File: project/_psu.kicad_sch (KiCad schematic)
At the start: 45 parts, among them J301 5V, J302 24V, J303 3V3, U301 ME3121AM6G, U302 MT3406

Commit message: fixing silk and bom and generating prod/doc files
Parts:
- F301: jlc-part-type (none) -> E; lcsc# (none) -> C22378353
- J301, J302, J303: jlc-part-type (none) -> -; now in the parts list
- L301, L302: jlc-part-type (none) -> E; lcsc# (none) -> C241467
- R301, R302, R312: jlc-part-type B -> E; lcsc# (none) -> C127687
- R303: lcsc# (none) -> C17470
- R304, R313, R314, R316: lcsc# (none) -> C17713
- R305, R306, R307, R315: lcsc# (none) -> C17414
- R308, R309, R310, R311: lcsc# (none) -> C17673
- U302: jlc-part-type (none) -> E; lcsc# (none) -> C22462728

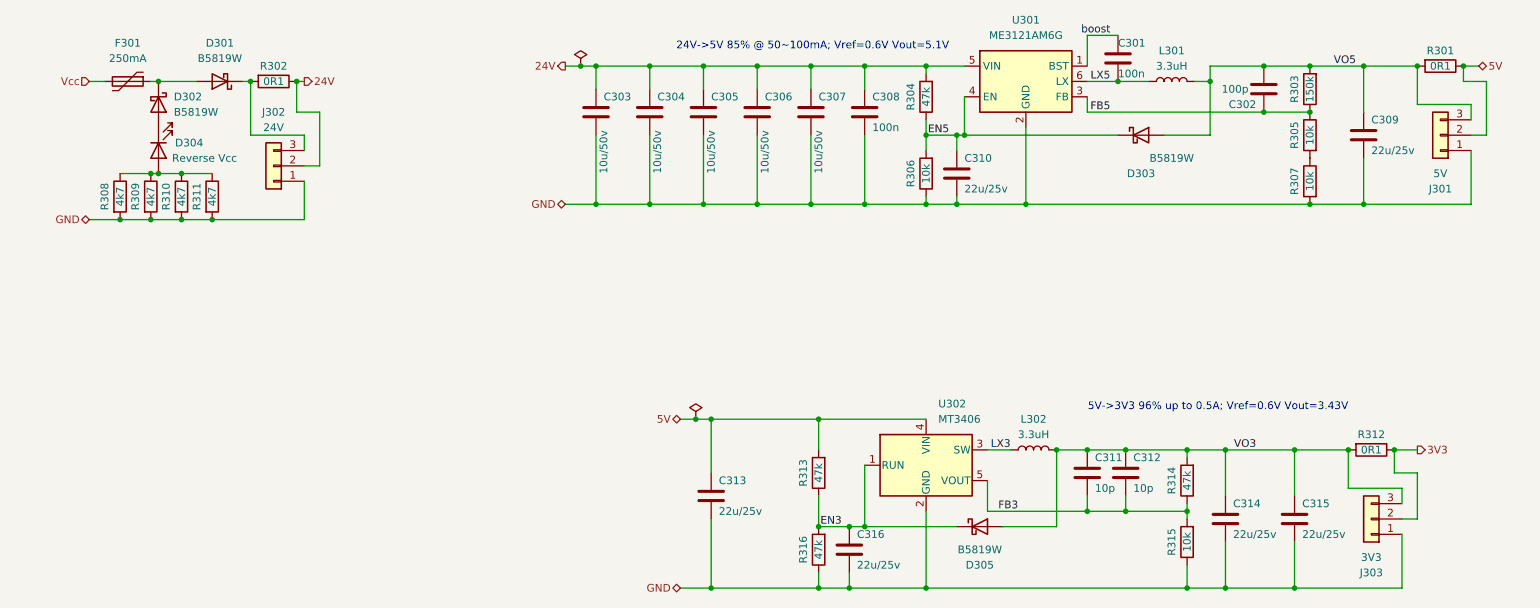
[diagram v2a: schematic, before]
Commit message: improvements for next prototype
* buck makes 6v now
* using LDO for 5v with over voltage disable
* using LDO for 3v3
* adding zener to 24v led to stop it from glowing from 5v USB
* added 0.2mm heigt for USB port hole
* both buttons now 15mm height
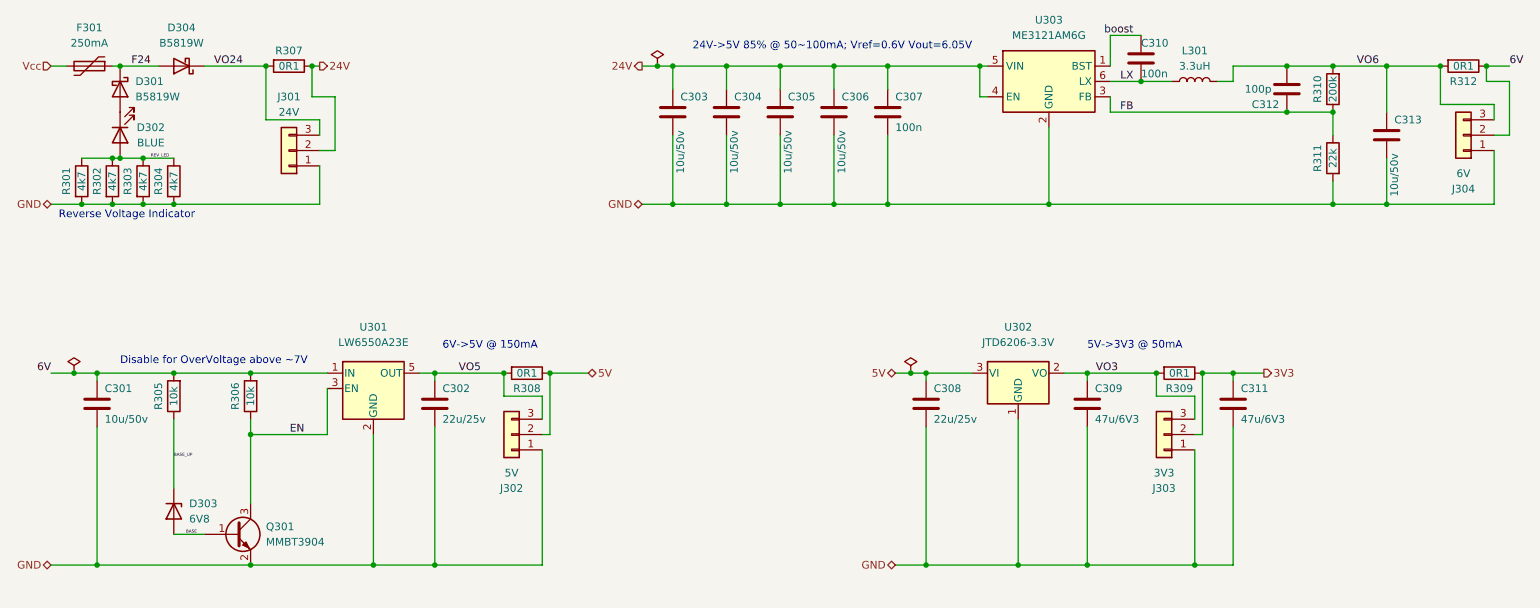
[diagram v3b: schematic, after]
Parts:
- removed C305: 10u/50v, Capacitor_SMD:C_0805_2012Metric_Pad1.18x1.45mm_HandSolder, symbol Device:C
- removed C310, C314, C315, C316: 22u/25v, Capacitor_SMD:C_0805_2012Metric_Pad1.18x1.45mm_HandSolder, symbol Device:C
- removed C312: 10p, Capacitor_SMD:C_0805_2012Metric_Pad1.18x1.45mm_HandSolder, symbol Device:C
- removed D303, D305: B5819W, Diode_SMD:D_SOD-123, symbol Device:D_Schottky
- removed L302: 3.3uH, Inductor_SMD:L_1008_2520Metric_Pad1.43x2.20mm_HandSolder, symbol Device:L
- removed R304, R313, R314, R316: 47k, Resistor_SMD:R_0805_2012Metric_Pad1.20x1.40mm_HandSolder, symbol Device:R
- removed R312: 0R1, Resistor_SMD:R_0805_2012Metric_Pad1.20x1.40mm_HandSolder, symbol Device:R
- removed R315: 10k, Resistor_SMD:R_0805_2012Metric_Pad1.20x1.40mm_HandSolder, symbol Device:R
- removed U302: MT3406, Package_TO_SOT_SMD:TSOT-23-5, symbol Regulator_Switching:LTC3406ES5
- added C301: 10u/50v, Capacitor_SMD:C_0805_2012Metric_Pad1.18x1.45mm_HandSolder, symbol Device:C
- added C302, C308: 22u/25v, Capacitor_SMD:C_0805_2012Metric_Pad1.18x1.45mm_HandSolder, symbol Device:C
- added D303: 6V8, Diode_SMD:D_SOD-323_HandSoldering, symbol Device:D_Zener
- added J302: 5V, Connector_PinHeader_2.54mm:PinHeader_1x03_P2.54mm_Vertical, symbol Connector_Generic:Conn_01x03
- added Q301: MMBT3904, Package_TO_SOT_SMD:SOT-23, symbol Device:Q_NPN_BEC
- added R308, R309: 0R1, Resistor_SMD:R_0805_2012Metric_Pad1.20x1.40mm_HandSolder, symbol Device:R
- added U301: LW6550A23E, Package_TO_SOT_SMD:SOT-23-5, symbol Regulator_Linear:TLV71209_SOT23-5
- added U302: JTD6206-3.3V, Package_TO_SOT_SMD:SOT-23, symbol Regulator_Linear:APE8865N-33-HF-3
- C309: value 22u/25v -> 47u/6V3; lcsc# C45783 -> C16780
- C311: value 10p -> 47u/6V3; lcsc# C1634 -> C16780
- C313: value 22u/25v -> 10u/50v; lcsc# C45783 -> C440198
- D302: renamed from D304; value Reverse Vcc -> BLUE
- J304: renamed from J301; value 5V -> 6V
- L301: lcsc# C241467 -> C5832373
- R310: renamed from R303; value 150k -> 200k; lcsc# C17470 -> C17539
- R311: renamed from R307; value 10k -> 22k; lcsc# C17414 -> C17560
- renumbered C306 to C305, C307 to C306, C308 to C307, C301 to C310, C302 to C312, D302 to D301, D301 to D304, J302 to J301, R308 to R301, R309 to R302, R310 to R303, R311 to R304, R302 to R307, R301 to R312, U301 to U303
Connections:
- net FB3 is gone; now on net GND: C311.2
- net 24V: now also U303.4 (EN)
- net 3V3: now also C311.1, R309.1
- net 5V: now also C308.1, J302.2 (Pin_2), R308.1, U302.3 (VI); no longer C313.1, J304.2 (Pin_2), R312.1
- net GND: now also C301.2, C302.2, C308.2, J302.1 (Pin_1), Q301.2 (E), U301.2 (GND), U302.1 (GND); no longer R306.1
- net VO3: now also C309.1, R309.2, U302.2 (VO); no longer C311.1
- net VO5: now also C302.1, J302.3 (Pin_3), R308.2, U301.5 (OUT); no longer C309.1, C312.2, J304.3 (Pin_3), L301.2, R310.2, R312.2
- net REV_LED: now reaches D302.2 (A), R301.1, R302.1, R303.1, R304.1
- net F24: now reaches D301.1 (K), D304.2 (A), F301.1
- net VO24: now reaches D304.1 (K), J301.3 (Pin_3), R307.2
- net 6V: now reaches R305.2
- net 6V: now also J304.2 (Pin_2), R306.2, R312.1, C301.1, U301.1 (IN); no longer R311.1
- removed net EN5: R306.2, U303.4 (EN)
- net FB5 renamed FB
- net FB: now also R311.1; no longer R305.1
- net LX5 renamed LX
- new net BASE: D303.2 (A), Q301.1 (B)
- new net BASE_UP: D303.1 (K), R305.1
- new net EN: Q301.3 (C), R306.1, U301.3 (EN)
- new net VO6: C312.2, C313.1, J304.3 (Pin_3), L301.2, R310.2, R312.2
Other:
- note added: "24V->5V 85% @ 50~100mA; Vref=0.6V Vout=6.05V"
- note added: "5V->3V3 @ 50mA"
- note added: "6V->5V @ 150mA"
- note added: "Disable for OverVoltage above ~7V"
- note added: "Reverse Voltage Indicator"
- note removed: "24V->5V 85% @ 50~100mA; Vref=0.6V Vout=5.1V"
- note removed: "5V->3V3 96% up to 0.5A; Vref=0.6V Vout=3.43V"
- moved on the sheet: C303, C304, C305, C306, C307, C310, C312, D301, D302, D304, F301, J301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
